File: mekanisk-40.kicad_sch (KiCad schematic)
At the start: 135 parts, among them J1 USB_C_Receptacle_USB2.0, Q1 2N7002, SW1 RST, U2 USBLC6-2SC6, U3 STM32F072C8Tx, U4 XC6206PxxxMR-Regulator_Linear

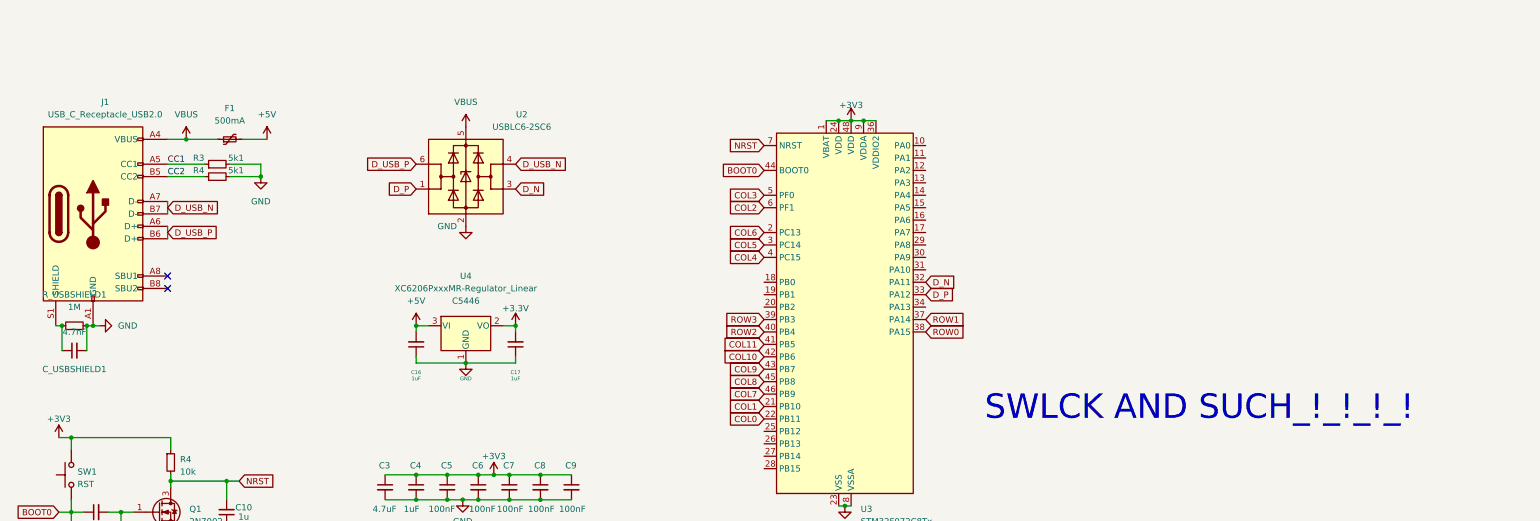
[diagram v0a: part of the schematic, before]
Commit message: minimal gnd fill, added jst pico footprints
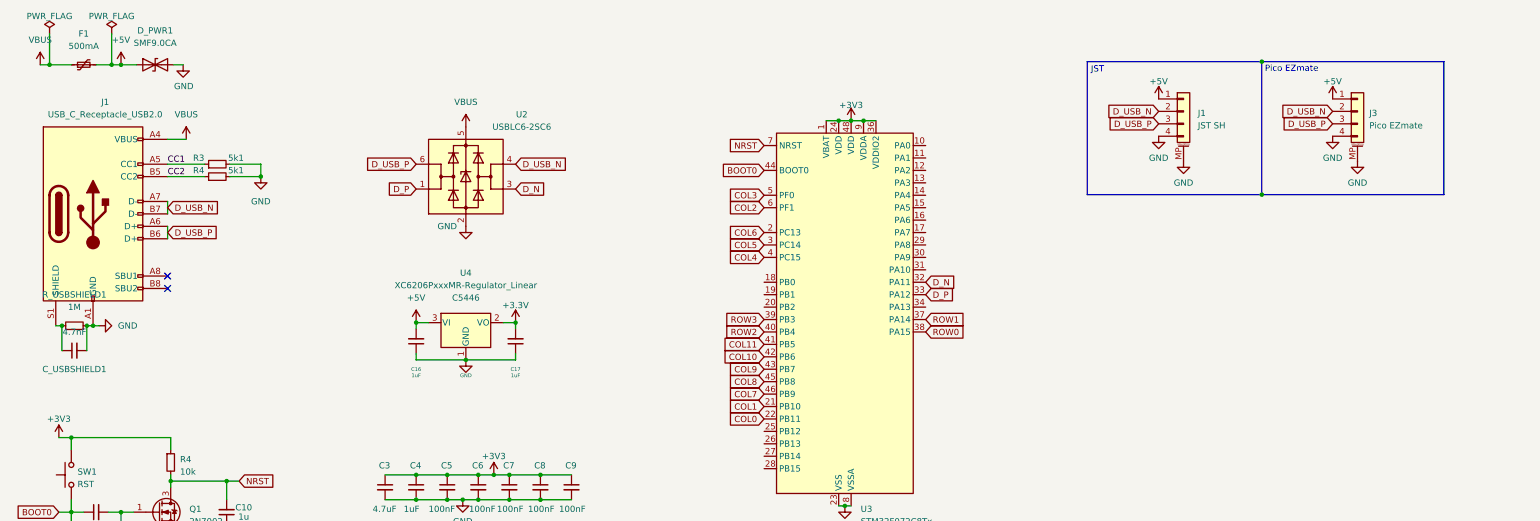
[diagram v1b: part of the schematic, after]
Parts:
- added D_PWR1: SMF9.0CA, Diode_SMD:D_SOD-123, symbol Device:D_TVS
- added J1: JST SH, Connector_JST:JST_SH_SM04B-SRSS-TB_1x04-1MP_P1.00mm_Horizontal, symbol Connector_Generic_MountingPin:Conn_01x04_MountingPin
- added J3: Pico EZmate, Connector_Molex:Molex_Pico-EZmate_78171-0004_1x04-1MP_P1.20mm_Vertical, symbol Connector_Generic_MountingPin:Conn_01x04_MountingPin
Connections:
- net +5V: now also D_PWR1.1 (A1), J1.1 (Pin_1), J3.1 (Pin_1)
- net D_USB_N: now also J1.2 (Pin_2), J3.2 (Pin_2)
- net D_USB_P: now also J1.3 (Pin_3), J3.3 (Pin_3)
- net GND: now also D_PWR1.2 (A2), J1.4 (Pin_4), J1.MP (MountPin), J3.4 (Pin_4), J3.MP (MountPin)
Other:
- note added: "JST"
- note added: "Pico EZmate"
- note removed: "SWLCK AND SUCH_!_!_!_!"
- moved on the sheet: C16, C17, F1, U4

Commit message: slight routing change, necessary?
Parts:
- C10: value 1u -> 1uF
- C11: value 4.7u -> 4.7uF
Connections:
- net COL10: now also U3.43 (PB7); no longer U3.42 (PB6)
- net COL11: now also U3.42 (PB6); no longer U3.41 (PB5)
- net COL2: now also U3.13 (PA3); no longer U3.6 (PF1)
- net COL3: now also U3.12 (PA2); no longer U3.5 (PF0)
- net COL4: now also U3.11 (PA1); no longer U3.4 (PC15)
- net COL5: now also U3.10 (PA0); no longer U3.3 (PC14)
- net COL6: now also U3.6 (PF1); no longer U3.2 (PC13)
- net COL7: now also U3.5 (PF0); no longer U3.46 (PB9)
- net COL8: now also U3.46 (PB9); no longer U3.45 (PB8)
- net COL9: now also U3.45 (PB8); no longer U3.43 (PB7)
- net ROW0: now also U3.39 (PB3); no longer U3.38 (PA15)
- net ROW2: now also U3.41 (PB5); no longer U3.40 (PB4)
- net ROW3: now also U3.40 (PB4); no longer U3.39 (PB3)
- no-connect marks 2 -> 7
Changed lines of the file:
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@@
   (junction (at 50.165 118.11) (diameter 0) (color 0 0 0 0)
   )
+  (no_connect (at 181.61 60.96))
+  (no_connect (at 181.61 66.04))
   (no_connect (at 59.69 72.39))
   (no_connect (at 59.69 69.85))
+  (no_connect (at 181.61 63.5))
+  (no_connect (at 214.63 76.2))
+  (no_connect (at 214.63 81.28))
   (wire (pts (xy 186.055 241.3) (xy 198.755 241.3))
     (stroke (width 0) (type default))
@@
     )
   )
-  (global_label "COL6" (shape input) (at 181.61 60.96 180) (fields_autoplaced)
+  (global_label "COL6" (shape input) (at 181.61 55.88 180) (fields_autoplaced)
     (effects (font (size 1.27 1.27)) (justify right))
-    (property "Intersheetrefs" "${INTERSHEET_REFS}" (at 173.8661 60.96 0)
+    (property "Intersheetrefs" "${INTERSHEET_REFS}" (at 173.8661 55.88 0)
       (effects (font (size 1.27 1.27)) (justify right) hide)
     )
   )
-  (global_label "ROW3" (shape input) (at 181.61 78.74 180) (fields_autoplaced)
+  (global_label "ROW3" (shape input) (at 181.61 81.28 180) (fields_autoplaced)
     (effects (font (size 1.27 1.27)) (justify right))
-    (property "Intersheetrefs" "${INTERSHEET_REFS}" (at 173.4428 78.74 0)
+    (property "Intersheetrefs" "${INTERSHEET_REFS}" (at 173.4428 81.28 0)
       (effects (font (size 1.27 1.27)) (justify right) hide)
     )
@@
     )
   )
-  (global_label "ROW0" (shape input) (at 214.63 81.28 0) (fields_autoplaced)
-    (effects (font (size 1.27 1.27)) (justify left))
-    (property "Intersheetrefs" "${INTERSHEET_REFS}" (at 222.7972 81.28 0)
-      (effects (font (size 1.27 1.27)) (justify left) hide)
-    )
-  )
-  (global_label "COL2" (shape input) (at 181.61 55.88 180) (fields_autoplaced)
+  (global_label "ROW0" (shape input) (at 181.61 78.74 180) (fields_autoplaced)
     (effects (font (size 1.27 1.27)) (justify right))
-    (property "Intersheetrefs" "${INTERSHEET_REFS}" (at 173.8661 55.88 0)
+    (property "Intersheetrefs" "${INTERSHEET_REFS}" (at 173.4428 78.74 0)
       (effects (font (size 1.27 1.27)) (justify right) hide)
     )
   )
+  (global_label "COL2" (shape input) (at 214.63 50.8 0) (fields_autoplaced)
+    (effects (font (size 1.27 1.27)) (justify left))
+    (property "Intersheetrefs" "${INTERSHEET_REFS}" (at 222.3739 50.8 0)
+      (effects (font (size 1.27 1.27)) (justify left) hide)
+    )
+  )
   (global_label "COL4" (shape input) (at 130.81 172.72 90) (fields_autoplaced)
     (effects (font (size 1.27 1.27)) (justify left))
@@
     )
   )
-  (global_label "COL7" (shape input) (at 181.61 93.98 180) (fields_autoplaced)
+  (global_label "COL7" (shape input) (at 181.61 53.34 180) (fields_autoplaced)
     (effects (font (size 1.27 1.27)) (justify right))
-    (property "Intersheetrefs" "${INTERSHEET_REFS}" (at 173.8661 93.98 0)
+    (property "Intersheetrefs" "${INTERSHEET_REFS}" (at 173.8661 53.34 0)
       (effects (font (size 1.27 1.27)) (justify right) hide)
     )
@@
     )
   )
-  (global_label "COL8" (shape input) (at 181.61 91.44 180) (fields_autoplaced)
+  (global_label "COL8" (shape input) (at 181.61 93.98 180) (fields_autoplaced)
     (effects (font (size 1.27 1.27)) (justify right))
-    (property "Intersheetrefs" "${INTERSHEET_REFS}" (at 173.8661 91.44 0)
+    (property "Intersheetrefs" "${INTERSHEET_REFS}" (at 173.8661 93.98 0)
       (effects (font (size 1.27 1.27)) (justify right) hide)
     )
@@
     )
   )
-  (global_label "COL11" (shape input) (at 181.61 83.82 180) (fields_autoplaced)
+  (global_label "COL11" (shape input) (at 181.61 86.36 180) (fields_autoplaced)
     (effects (font (size 1.27 1.27)) (justify right))
-    (property "Intersheetrefs" "${INTERSHEET_REFS}" (at 172.6566 83.82 0)
+    (property "Intersheetrefs" "${INTERSHEET_REFS}" (at 172.6566 86.36 0)
       (effects (font (size 1.27 1.27)) (justify right) hide)
     )
@@
     )
   )
-  (global_label "COL9" (shape input) (at 181.61 88.9 180) (fields_autoplaced)
+  (global_label "COL9" (shape input) (at 181.61 91.44 180) (fields_autoplaced)
     (effects (font (size 1.27 1.27)) (justify right))
-    (property "Intersheetrefs" "${INTERSHEET_REFS}" (at 173.8661 88.9 0)
+    (property "Intersheetrefs" "${INTERSHEET_REFS}" (at 173.8661 91.44 0)
       (effects (font (size 1.27 1.27)) (justify right) hide)
     )
   )
-  (global_label "COL3" (shape input) (at 181.61 53.34 180) (fields_autoplaced)
-    (effects (font (size 1.27 1.27)) (justify right))
-    (property "Intersheetrefs" "${INTERSHEET_REFS}" (at 173.8661 53.34 0)
-      (effects (font (size 1.27 1.27)) (justify right) hide)
+  (global_label "COL3" (shape input) (at 214.63 48.26 0) (fields_autoplaced)
+    (effects (font (size 1.27 1.27)) (justify left))
+    (property "Intersheetrefs" "${INTERSHEET_REFS}" (at 222.3739 48.26 0)
+      (effects (font (size 1.27 1.27)) (justify left) hide)
     )
   )
@@
     )
   )
-  (global_label "COL10" (shape input) (at 181.61 86.36 180) (fields_autoplaced)
+  (global_label "COL10" (shape input) (at 181.61 88.9 180) (fields_autoplaced)
     (effects (font (size 1.27 1.27)) (justify right))
-    (property "Intersheetrefs" "${INTERSHEET_REFS}" (at 172.6566 86.36 0)
+    (property "Intersheetrefs" "${INTERSHEET_REFS}" (at 172.6566 88.9 0)
       (effects (font (size 1.27 1.27)) (justify right) hide)
     )
   )
-  (global_label "COL5" (shape input) (at 181.61 63.5 180) (fields_autoplaced)
-    (effects (font (size 1.27 1.27)) (justify right))
-    (property "Intersheetrefs" "${INTERSHEET_REFS}" (at 173.8661 63.5 0)
-      (effects (font (size 1.27 1.27)) (justify right) hide)
+  (global_label "COL5" (shape input) (at 214.63 43.18 0) (fields_autoplaced)
+    (effects (font (size 1.27 1.27)) (justify left))
+    (property "Intersheetrefs" "${INTERSHEET_REFS}" (at 222.3739 43.18 0)
+      (effects (font (size 1.27 1.27)) (justify left) hide)
     )
   )
@@
     )
   )
-  (global_label "COL4" (shape input) (at 181.61 66.04 180) (fields_autoplaced)
-    (effects (font (size 1.27 1.27)) (justify right))
-    (property "Intersheetrefs" "${INTERSHEET_REFS}" (at 173.8661 66.04 0)
-      (effects (font (size 1.27 1.27)) (justify right) hide)
+  (global_label "COL4" (shape input) (at 214.63 45.72 0) (fields_autoplaced)
+    (effects (font (size 1.27 1.27)) (justify left))
+    (property "Intersheetrefs" "${INTERSHEET_REFS}" (at 222.3739 45.72 0)
+      (effects (font (size 1.27 1.27)) (justify left) hide)
     )
   )
-  (global_label "ROW2" (shape input) (at 181.61 81.28 180) (fields_autoplaced)
+  (global_label "ROW2" (shape input) (at 181.61 83.82 180) (fields_autoplaced)
     (effects (font (size 1.27 1.27)) (justify right))
-    (property "Intersheetrefs" "${INTERSHEET_REFS}" (at 173.4428 81.28 0)
+    (property "Intersheetrefs" "${INTERSHEET_REFS}" (at 173.4428 83.82 0)
       (effects (font (size 1.27 1.27)) (justify right) hide)
     )
@@
       (effects (font (size 1.27 1.27)))
     )
-    (property "Value" "4.7u" (at 45.085 123.19 90)
+    (property "Value" "4.7uF" (at 45.085 123.19 90)
       (effects (font (size 1.27 1.27)))
     )
@@
       (effects (font (size 1.27 1.27)))
     )
-    (property "Value" "1u" (at 75.2475 119.0625 0)
+    (property "Value" "1uF" (at 75.2475 119.0625 0)
       (effects (font (size 1.27 1.27)))
     )
